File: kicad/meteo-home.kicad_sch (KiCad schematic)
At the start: 17 parts, among them J1 S 4

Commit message: Feat: i2c connectors pins and disposition changed
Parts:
- removed I2C3: I2C 3, Connector_JST:JST_SH_SM04B-SRSS-TB_1x04-1MP_P1.00mm_Horizontal, symbol Connector_Generic_MountingPin:Conn_01x04_MountingPin
- removed I2C4: I2C 4, Connector_JST:JST_SH_SM04B-SRSS-TB_1x04-1MP_P1.00mm_Horizontal, symbol Connector_Generic_MountingPin:Conn_01x04_MountingPin
- added I2C3: I2C 3, Connector_PinSocket_1.00mm:PinSocket_1x04_P1.00mm_Vertical, symbol Connector:Conn_01x04_Socket
- added I2C4: I2C 4, Connector_PinSocket_1.00mm:PinSocket_1x04_P1.00mm_Vertical, symbol Connector:Conn_01x04_Socket
- Tx1: footprint Connector_Molex:Molex_SL_171971-0002_1x02_P2.54mm_Vertical -> Connector_PinSocket_2.54mm:PinSocket_1x02_P2.54mm_Vertical
- renumbered TH1 to DHT22
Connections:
- net +5V is gone; now on net VCC: J1.1 (Pin_1), PWR1.1 (Pin_1)
- net +3V3: now also A1.2 (Pin_2); no longer A1.1 (Pin_1)
- net A0: now also A1.1 (Pin_1); no longer A1.2 (Pin_2)
- net GND: now also I2C3.1 (Pin_1), I2C4.1 (Pin_1)
- net SCL: now also I2C1.3 (Pin_3), I2C2.3 (Pin_3), I2C3.3 (Pin_3), I2C4.3 (Pin_3); no longer I2C1.4 (Pin_4), I2C2.4 (Pin_4)
- net SDA: now also I2C1.4 (Pin_4), I2C2.4 (Pin_4), I2C3.4 (Pin_4), I2C4.4 (Pin_4); no longer I2C1.3 (Pin_3), I2C2.3 (Pin_3)
- net VCC: now also I2C3.2 (Pin_2), I2C4.2 (Pin_2)

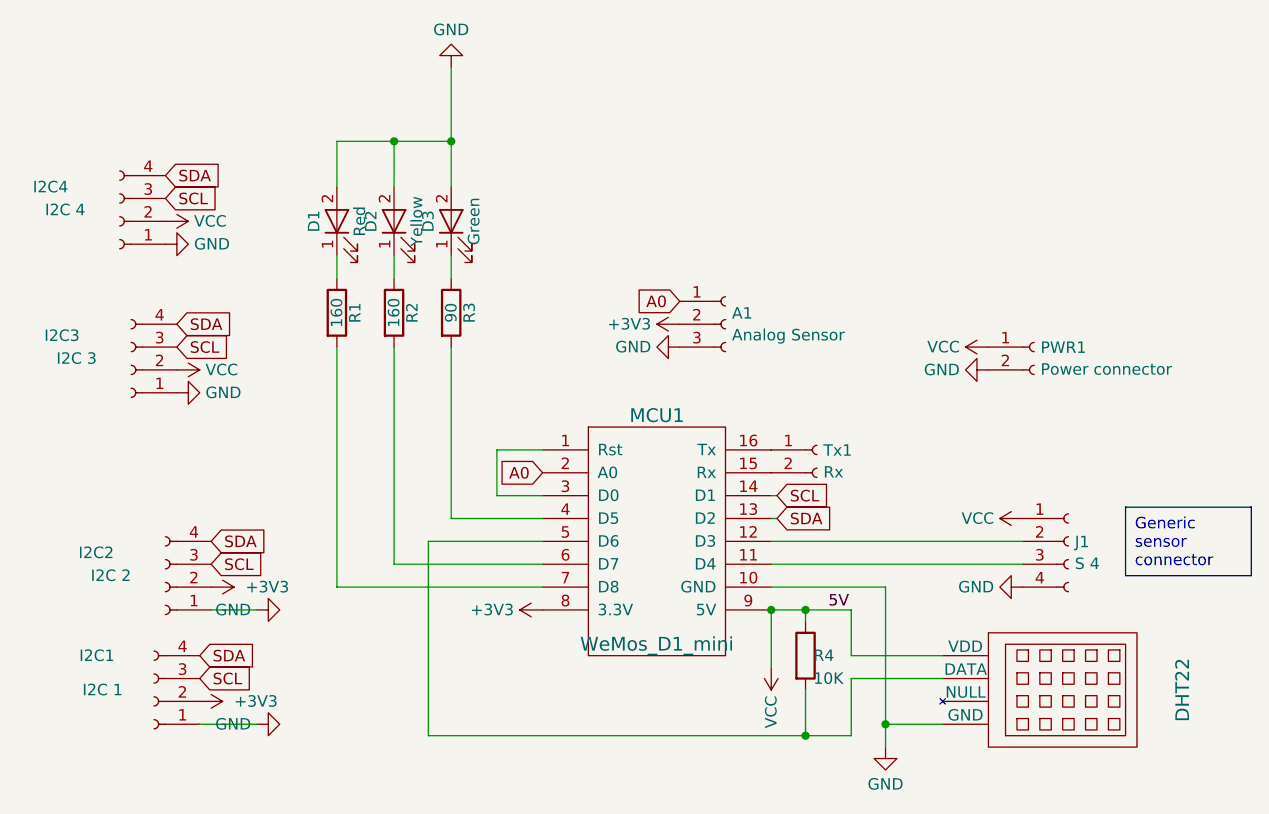
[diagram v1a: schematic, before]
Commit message: Fix: connectors relocation
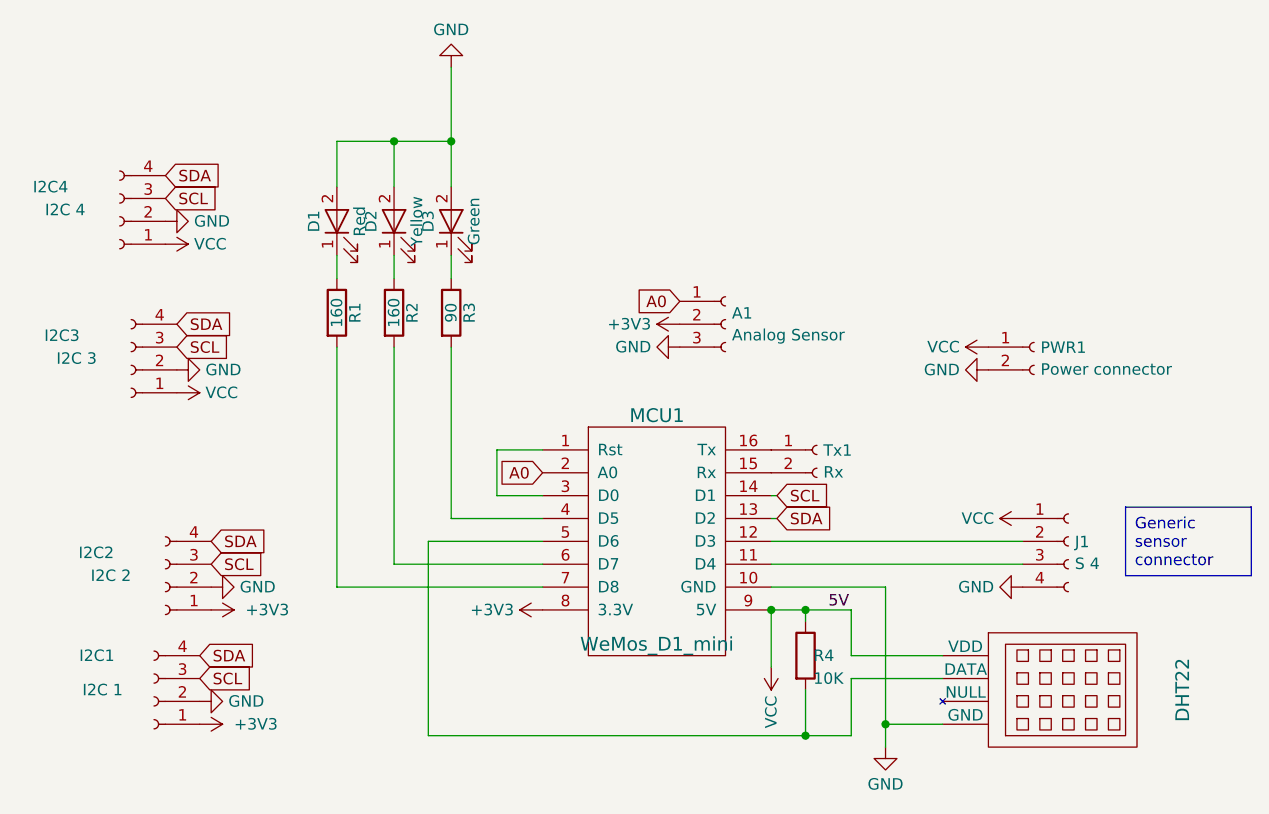
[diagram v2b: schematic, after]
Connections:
- net +3V3: now also I2C1.1 (Pin_1), I2C2.1 (Pin_1); no longer I2C1.2 (Pin_2), I2C2.2 (Pin_2)
- net GND: now also I2C1.2 (Pin_2), I2C2.2 (Pin_2), I2C3.2 (Pin_2), I2C4.2 (Pin_2); no longer I2C1.1 (Pin_1), I2C2.1 (Pin_1), I2C3.1 (Pin_1), I2C4.1 (Pin_1)
- net VCC: now also I2C3.1 (Pin_1), I2C4.1 (Pin_1); no longer I2C3.2 (Pin_2), I2C4.2 (Pin_2)
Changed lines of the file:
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@@
-    (stroke (width 0) (type default))
-  )
-  (wire (pts (xy 67.31 99.06) (xy 60.96 99.06))
     (stroke (width 0) (type default))
   )
@@
   )
   (wire (pts (xy 99.06 81.28) (xy 82.55 81.28))
-    (stroke (width 0) (type default))
-  )
-  (wire (pts (xy 67.31 86.36) (xy 62.23 86.36))
     (stroke (width 0) (type default))
   )
@@
     )
   )
-  (symbol (lib_id "power:+3V3") (at 60.96 96.52 270) (unit 1)
-    (in_bom yes) (on_board yes) (dnp no)
-    (property "Reference" "#PWR014" (at 57.15 96.52 0)
-      (effects (font (size 1.27 1.27)) hide)
-    )
-    (property "Value" "+3V3" (at 64.77 96.52 90)
-      (effects (font (size 1.27 1.27)) (justify left))
-    )
-    (property "Footprint" "" (at 60.96 96.52 0)
-      (effects (font (size 1.27 1.27)) hide)
-    )
-    (property "Datasheet" "" (at 60.96 96.52 0)
+  (symbol (lib_id "power:+3V3") (at 60.96 99.06 270) (unit 1)
+    (in_bom yes) (on_board yes) (dnp no)
+    (property "Reference" "#PWR014" (at 57.15 99.06 0)
+      (effects (font (size 1.27 1.27)) hide)
+    )
+    (property "Value" "+3V3" (at 64.77 99.06 90)
+      (effects (font (size 1.27 1.27)) (justify left))
+    )
+    (property "Footprint" "" (at 60.96 99.06 0)
+      (effects (font (size 1.27 1.27)) hide)
+    )
+    (property "Datasheet" "" (at 60.96 99.06 0)
       (effects (font (size 1.27 1.27)) hide)
     )
@@
     )
   )
-  (symbol (lib_id "power:GND") (at 57.15 45.72 90) (unit 1)
-    (in_bom yes) (on_board yes) (dnp no) (fields_autoplaced)
-    (property "Reference" "#PWR018" (at 63.5 45.72 0)
-      (effects (font (size 1.27 1.27)) hide)
-    )
-    (property "Value" "GND" (at 60.3249 45.72 90)
+  (symbol (lib_id "power:GND") (at 57.15 43.18 90) (unit 1)
+    (in_bom yes) (on_board yes) (dnp no) (fields_autoplaced)
+    (property "Reference" "#PWR018" (at 63.5 43.18 0)
+      (effects (font (size 1.27 1.27)) hide)
+    )
+    (property "Value" "GND" (at 60.3249 43.18 90)
       (effects (font (size 1.27 1.27)) (justify right))
     )
-    (property "Footprint" "" (at 57.15 45.72 0)
-      (effects (font (size 1.27 1.27)) hide)
-    )
-    (property "Datasheet" "" (at 57.15 45.72 0)
+    (property "Footprint" "" (at 57.15 43.18 0)
+      (effects (font (size 1.27 1.27)) hide)
+    )
+    (property "Datasheet" "" (at 57.15 43.18 0)
       (effects (font (size 1.27 1.27)) hide)
     )
@@
     )
   )
-  (symbol (lib_id "power:GND") (at 67.31 86.36 90) (unit 1)
-    (in_bom yes) (on_board yes) (dnp no) (fields_autoplaced)
-    (property "Reference" "#PWR01" (at 73.66 86.36 0)
-      (effects (font (size 1.27 1.27)) hide)
-    )
-    (property "Value" "GND" (at 66.675 86.36 90)
-      (effects (font (size 1.27 1.27)) (justify left))
-    )
-    (property "Footprint" "" (at 67.31 86.36 0)
-      (effects (font (size 1.27 1.27)) hide)
-    )
-    (property "Datasheet" "" (at 67.31 86.36 0)
+  (symbol (lib_id "power:GND") (at 62.23 83.82 90) (unit 1)
+    (in_bom yes) (on_board yes) (dnp no) (fields_autoplaced)
+    (property "Reference" "#PWR01" (at 68.58 83.82 0)
+      (effects (font (size 1.27 1.27)) hide)
+    )
+    (property "Value" "GND" (at 65.405 83.82 90)
+      (effects (font (size 1.27 1.27)) (justify right))
+    )
+    (property "Footprint" "" (at 62.23 83.82 0)
+      (effects (font (size 1.27 1.27)) hide)
+    )
+    (property "Datasheet" "" (at 62.23 83.82 0)
       (effects (font (size 1.27 1.27)) hide)
     )
@@
     )
   )
-  (symbol (lib_id "power:GND") (at 67.31 99.06 90) (unit 1)
-    (in_bom yes) (on_board yes) (dnp no) (fields_autoplaced)
-    (property "Reference" "#PWR08" (at 73.66 99.06 0)
-      (effects (font (size 1.27 1.27)) hide)
-    )
-    (property "Value" "GND" (at 66.675 99.06 90)
-      (effects (font (size 1.27 1.27)) (justify left))
-    )
-    (property "Footprint" "" (at 67.31 99.06 0)
-      (effects (font (size 1.27 1.27)) hide)
-    )
-    (property "Datasheet" "" (at 67.31 99.06 0)
+  (symbol (lib_id "power:GND") (at 60.96 96.52 90) (unit 1)
+    (in_bom yes) (on_board yes) (dnp no) (fields_autoplaced)
+    (property "Reference" "#PWR08" (at 67.31 96.52 0)
+      (effects (font (size 1.27 1.27)) hide)
+    )
+    (property "Value" "GND" (at 64.135 96.52 90)
+      (effects (font (size 1.27 1.27)) (justify right))
+    )
+    (property "Footprint" "" (at 60.96 96.52 0)
+      (effects (font (size 1.27 1.27)) hide)
+    )
+    (property "Datasheet" "" (at 60.96 96.52 0)
       (effects (font (size 1.27 1.27)) hide)
     )
@@
     )
   )
-  (symbol (lib_id "power:VCC") (at 57.15 43.18 270) (unit 1)
-    (in_bom yes) (on_board yes) (dnp no)
-    (property "Reference" "#PWR019" (at 53.34 43.18 0)
-      (effects (font (size 1.27 1.27)) hide)
-    )
-    (property "Value" "VCC" (at 60.325 43.18 90)
-      (effects (font (size 1.27 1.27)) (justify left))
-    )
-    (property "Footprint" "" (at 57.15 43.18 0)
-      (effects (font (size 1.27 1.27)) hide)
-    )
-    (property "Datasheet" "" (at 57.15 43.18 0)
+  (symbol (lib_id "power:VCC") (at 57.15 45.72 270) (unit 1)
+    (in_bom yes) (on_board yes) (dnp no)
+    (property "Reference" "#PWR019" (at 53.34 45.72 0)
+      (effects (font (size 1.27 1.27)) hide)
+    )
+    (property "Value" "VCC" (at 60.325 45.72 90)
+      (effects (font (size 1.27 1.27)) (justify left))
+    )
+    (property "Footprint" "" (at 57.15 45.72 0)
+      (effects (font (size 1.27 1.27)) hide)
+    )
+    (property "Datasheet" "" (at 57.15 45.72 0)
       (effects (font (size 1.27 1.27)) hide)
     )
@@
     )
   )
-  (symbol (lib_id "power:VCC") (at 58.42 59.69 270) (unit 1)
-    (in_bom yes) (on_board yes) (dnp no)
-    (property "Reference" "#PWR03" (at 54.61 59.69 0)
-      (effects (font (size 1.27 1.27)) hide)
-    )
-    (property "Value" "VCC" (at 61.595 59.69 90)
-      (effects (font (size 1.27 1.27)) (justify left))
+  (symbol (lib_id "power:VCC") (at 58.42 62.23 270) (unit 1)
+    (in_bom yes) (on_board yes) (dnp no)
+    (property "Reference" "#PWR03" (at 54.61 62.23 0)
+      (effects (font (size 1.27 1.27)) hide)
+    )
+    (property "Value" "VCC" (at 61.595 62.23 90)
+      (effects (font (size 1.27 1.27)) (justify left))
+    )
+    (property "Footprint" "" (at 58.42 62.23 0)
+      (effects (font (size 1.27 1.27)) hide)
+    )
+    (property "Datasheet" "" (at 58.42 62.23 0)
+      (effects (font (size 1.27 1.27)) hide)
+    )
+    (pin "1")
+    (instances
+      (project "meteo-home"
+        (path "/3f48dc18-b296-4c58-b04e-9a56011d842f"
+          (reference "#PWR03") (unit 1)
+        )
+      )
+    )
+  )
+  (symbol (lib_id "power:GND") (at 58.42 59.69 90) (unit 1)
+    (in_bom yes) (on_board yes) (dnp no) (fields_autoplaced)
+    (property "Reference" "#PWR015" (at 64.77 59.69 0)
+      (effects (font (size 1.27 1.27)) hide)
+    )
+    (property "Value" "GND" (at 61.595 59.69 90)
+      (effects (font (size 1.27 1.27)) (justify right))
     )
     (property "Footprint" "" (at 58.42 59.69 0)
@@
       (project "meteo-home"
         (path "/3f48dc18-b296-4c58-b04e-9a56011d842f"
-          (reference "#PWR03") (unit 1)
-        )
-      )
-    )
-  )
-  (symbol (lib_id "power:GND") (at 58.42 62.23 90) (unit 1)
-    (in_bom yes) (on_board yes) (dnp no) (fields_autoplaced)
-    (property "Reference" "#PWR015" (at 64.77 62.23 0)
-      (effects (font (size 1.27 1.27)) hide)
-    )
-    (property "Value" "GND" (at 61.595 62.23 90)
-      (effects (font (size 1.27 1.27)) (justify right))
-    )
-    (property "Footprint" "" (at 58.42 62.23 0)
-      (effects (font (size 1.27 1.27)) hide)
-    )
-    (property "Datasheet" "" (at 58.42 62.23 0)
-      (effects (font (size 1.27 1.27)) hide)
-    )
-    (pin "1")
-    (instances
-      (project "meteo-home"
-        (path "/3f48dc18-b296-4c58-b04e-9a56011d842f"
           (reference "#PWR015") (unit 1)
         )
@@
     )
   )
-  (symbol (lib_id "power:+3V3") (at 62.23 83.82 270) (unit 1)
-    (in_bom yes) (on_board yes) (dnp no)
-    (property "Reference" "#PWR011" (at 58.42 83.82 0)
-      (effects (font (size 1.27 1.27)) hide)
-    )
-    (property "Value" "+3V3" (at 66.04 83.82 90)
-      (effects (font (size 1.27 1.27)) (justify left))
-    )
-    (property "Footprint" "" (at 62.23 83.82 0)
-      (effects (font (size 1.27 1.27)) hide)
-    )
-    (property "Datasheet" "" (at 62.23 83.82 0)
-      (effects (font (size 1.27 1.27)) hide)
-    )
+  (symbol (lib_id "power:+3V3") (at 62.23 86.36 270) (unit 1)
+    (in_bom yes) (on_board yes) (dnp no)
+    (property "Reference" "#PWR011" (at 58.42 86.36 0)
+      (effects (font (size 1.27 1.27)) hide)
+    )
+    (property "Value" "+3V3" (at 66.04 86.36 90)
+      (effects (font (size 1.27 1.27)) (justify left))
+    )
+    (property "Footprint" "" (at 62.23 86.36 0)
+      (effects (font (size 1.27 1.27)) hide)
+    )
+    (property "Datasheet" "" (at 62.23 86.36 0)
+      (effects (font (size 1.27 1.27)) hide)
+    )
